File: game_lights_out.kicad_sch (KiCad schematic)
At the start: 91 parts, among them SW1 SW_MEC_5E, SW10 SW_MEC_5E, SW11 SW_MEC_5E, SW12 SW_MEC_5E, SW13 SW_MEC_5E, SW14 SW_MEC_5E, SW15 SW_MEC_5E, SW16 SW_MEC_5E, SW17 SW_MEC_5E, SW18 SW_MEC_5E, SW19 SW_MEC_5E, SW2 SW_MEC_5E, SW20 SW_MEC_5E, SW21 SW_MEC_5E, SW22 SW_MEC_5E, SW23 SW_MEC_5E, SW24 SW_MEC_5E, SW25 SW_MEC_5E, SW26 SW_MEC_5E, SW27 SW_MEC_5E, SW28 SW_MEC_5E, SW29 SW_MEC_5E, SW3 SW_MEC_5E, SW30 SW_MEC_5E, SW31 SW_MEC_5E, SW32 SW_MEC_5E, SW33 SW_MEC_5E, SW34 SW_MEC_5E, SW35 SW_MEC_5E, SW36 SW_MEC_5E, SW37 SW_MEC_5E, SW38 SW_MEC_5E, SW39 SW_MEC_5E, SW4 SW_MEC_5E, SW40 SW_MEC_5E, SW5 SW_MEC_5E, SW6 SW_MEC_5E, SW7 SW_MEC_5E, SW8 SW_MEC_5E, SW9 SW_MEC_5E, U1 ATmega328-P, U2 ULN2803A

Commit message: Added labels to programming pins and updated file format
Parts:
- D1, D10, D11, D12, D13, D14, D15, D16, D17, D18, D19, D2, D20, D21, D22, D23, D24, D25, D26, D27, D28, D29, D3, D30, D31, D32, D33, D34, D35, D36, D37, D38, D39, D4, D40, D5, D6, D7, D8, D9: footprint LED_THT:LED_D5.0mm_IRGrey -> LED_THT:LED_D5.0mm
- DMOD1, DMOD2: footprint LED_THT:LED_D5.0mm_IRGrey -> LED_THT:LED_D1.8mm_W3.3mm_H2.4mm

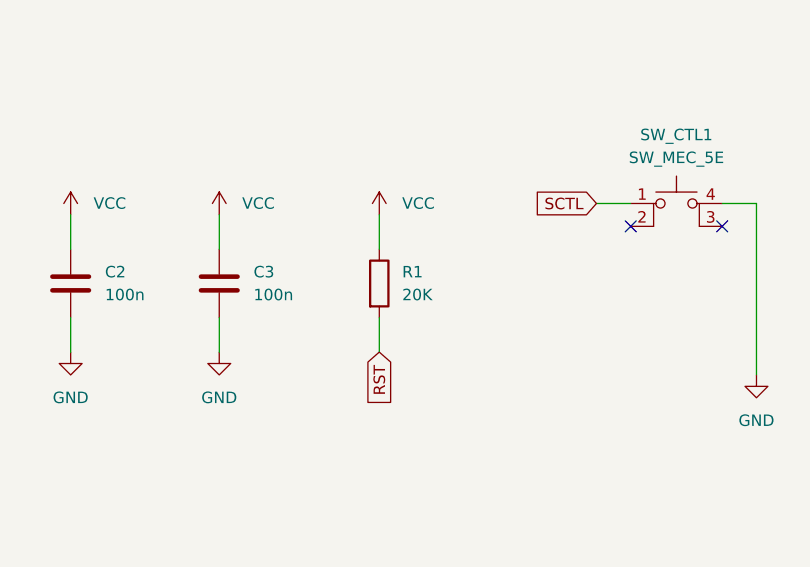
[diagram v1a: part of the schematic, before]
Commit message: Removed reset pin resistor
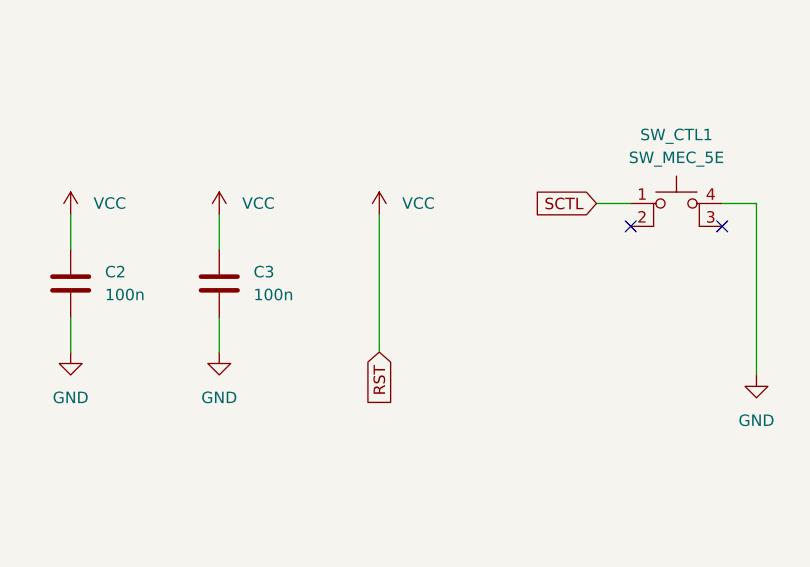
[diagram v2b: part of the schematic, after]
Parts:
- removed R1: 20K, Resistor_THT:R_Axial_DIN0207_L6.3mm_D2.5mm_P7.62mm_Horizontal, symbol Device:R
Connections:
- net RST is gone; now on net VCC: U1.1 (~{RESET}/PC6)
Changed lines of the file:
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@@
     (stroke (width 0) (type default))
   )
+  (wire (pts (xy 194.31 124.46) (xy 194.31 139.7))
+    (stroke (width 0) (type default))
+  )
   (wire (pts (xy 91.44 144.78) (xy 88.9 144.78))
     (stroke (width 0) (type default))
@@
     (stroke (width 0) (type default))
   )
-  (wire (pts (xy 194.31 135.89) (xy 194.31 139.7))
-    (stroke (width 0) (type default))
-  )
   (wire (pts (xy 53.34 129.54) (xy 50.8 129.54))
     (stroke (width 0) (type default))
@@
     (stroke (width 0) (type default))
   )
-  (wire (pts (xy 194.31 124.46) (xy 194.31 128.27))
-    (stroke (width 0) (type default))
-  )
   (wire (pts (xy 114.3 54.61) (xy 115.57 54.61))
     (stroke (width 0) (type default))
@@
         )
       )
-    )
-  )
-  (symbol (lib_id "Device:R") (at 194.31 132.08 0) (unit 1)
-    (in_bom yes) (on_board yes) (dnp no) (fields_autoplaced)
-    (property "Reference" "R1" (at 196.85 130.8099 0)
-      (effects (font (size 1.27 1.27)) (justify left))
-    )
-    (property "Value" "20K" (at 196.85 133.3499 0)
-      (effects (font (size 1.27 1.27)) (justify left))
-    )
-    (property "Footprint" "Resistor_THT:R_Axial_DIN0207_L6.3mm_D2.5mm_P7.62mm_Horizontal" (at 192.532 132.08 90)
-      (effects (font (size 1.27 1.27)) hide)
-    )
-    (property "Datasheet" "~" (at 194.31 132.08 0)
-      (effects (font (size 1.27 1.27)) hide)
-    )
-    (pin "1")
-    (pin "2")
-    (instances
-      (project "game_lights_out"
-        (path "/ccb92925-3037-4924-9354-2881b1b404a5"
-          (reference "R1") (unit 1)
-        )
-      )

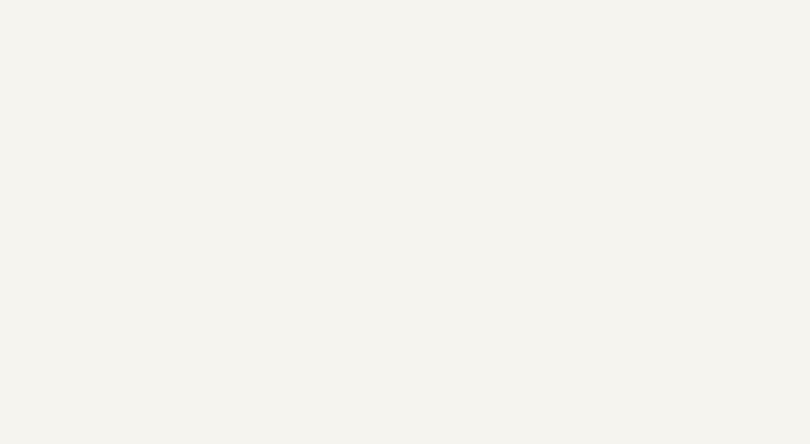
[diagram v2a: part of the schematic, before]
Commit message: Added mounting holes
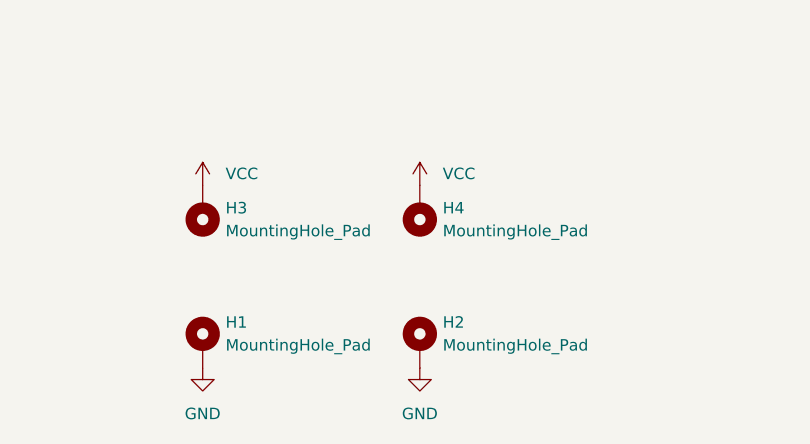
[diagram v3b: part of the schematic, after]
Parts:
- added H1, H2, H3, H4: MountingHole_Pad, MountingHole:MountingHole_2.5mm_Pad, symbol Mechanical:MountingHole_Pad
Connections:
- net GND: now also H1.1, H2.1
- net VCC: now also H3.1, H4.1
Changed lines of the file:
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@@
+    )
+  )
+  (symbol (lib_id "power:VCC") (at 143.51 170.18 0) (unit 1)
+    (in_bom yes) (on_board yes) (dnp no) (fields_autoplaced)
+    (property "Reference" "#PWR02" (at 143.51 173.99 0)
+      (effects (font (size 1.27 1.27)) hide)
+    )
+    (property "Value" "VCC" (at 146.05 168.9099 0)
+      (effects (font (size 1.27 1.27)) (justify left))
+    )
+    (property "Footprint" "" (at 143.51 170.18 0)
+      (effects (font (size 1.27 1.27)) hide)
+    )
+    (property "Datasheet" "" (at 143.51 170.18 0)
+      (effects (font (size 1.27 1.27)) hide)
+    )
+    (pin "1")
+    (instances
+      (project "game_lights_out"
+        (path "/ccb92925-3037-4924-9354-2881b1b404a5"
+          (reference "#PWR02") (unit 1)
+        )
+      )
     )
   )
@@
     )
   )
+  (symbol (lib_id "Mechanical:MountingHole_Pad") (at 143.51 187.96 0) (unit 1)
+    (in_bom yes) (on_board yes) (dnp no) (fields_autoplaced)
+    (property "Reference" "H2" (at 146.05 185.42 0)
+      (effects (font (size 1.27 1.27)) (justify left))
+    )
+    (property "Value" "MountingHole_Pad" (at 146.05 187.96 0)
+      (effects (font (size 1.27 1.27)) (justify left))
+    )
+    (property "Footprint" "MountingHole:MountingHole_2.5mm_Pad" (at 143.51 187.96 0)
+      (effects (font (size 1.27 1.27)) hide)
+    )
+    (property "Datasheet" "~" (at 143.51 187.96 0)
+      (effects (font (size 1.27 1.27)) hide)
+    )
+    (pin "1")
+    (instances
+      (project "game_lights_out"
+        (path "/ccb92925-3037-4924-9354-2881b1b404a5"
+          (reference "H2") (unit 1)
+        )
+      )
+    )
+  )
+  (symbol (lib_id "power:GND") (at 143.51 190.5 0) (unit 1)
+    (in_bom yes) (on_board yes) (dnp no) (fields_autoplaced)
+    (property "Reference" "#PWR04" (at 143.51 196.85 0)
+      (effects (font (size 1.27 1.27)) hide)
+    )
+    (property "Value" "GND" (at 143.51 195.58 0)
+      (effects (font (size 1.27 1.27)))
+    )
+    (property "Footprint" "" (at 143.51 190.5 0)
+      (effects (font (size 1.27 1.27)) hide)
+    )
+    (property "Datasheet" "" (at 143.51 190.5 0)
+      (effects (font (size 1.27 1.27)) hide)
+    )
+    (pin "1")
+    (instances
+      (project "game_lights_out"
+        (path "/ccb92925-3037-4924-9354-2881b1b404a5"
+          (reference "#PWR04") (unit 1)
+        )
+      )
+    )
+  )
   (symbol (lib_id "LED:CQY99") (at 241.3 53.34 270) (unit 1)
     (in_bom yes) (on_board yes) (dnp no) (fields_autoplaced)
@@
     )
   )
+  (symbol (lib_id "power:VCC") (at 119.38 170.18 0) (unit 1)
+    (in_bom yes) (on_board yes) (dnp no) (fields_autoplaced)
+    (property "Reference" "#PWR01" (at 119.38 173.99 0)
+      (effects (font (size 1.27 1.27)) hide)
+    )
+    (property "Value" "VCC" (at 121.92 168.9099 0)
+      (effects (font (size 1.27 1.27)) (justify left))
+    )
+    (property "Footprint" "" (at 119.38 170.18 0)
+      (effects (font (size 1.27 1.27)) hide)
+    )
+    (property "Datasheet" "" (at 119.38 170.18 0)
+      (effects (font (size 1.27 1.27)) hide)
+    )
+    (pin "1")
+    (instances
+      (project "game_lights_out"
+        (path "/ccb92925-3037-4924-9354-2881b1b404a5"
+          (reference "#PWR01") (unit 1)
+        )
+      )
+    )
+  )
   (symbol (lib_id "Switch:SW_MEC_5E") (at 54.61 71.12 0) (unit 1)
     (in_bom yes) (on_board yes) (dnp no) (fields_autoplaced)
@@
         (path "/ccb92925-3037-4924-9354-2881b1b404a5"
           (reference "D27") (unit 1)
+        )
+      )
+    )
+  )
+  (symbol (lib_id "Mechanical:MountingHole_Pad") (at 143.51 172.72 180) (unit 1)
+    (in_bom yes) (on_board yes) (dnp no) (fields_autoplaced)
+    (property "Reference" "H4" (at 146.05 172.72 0)
+      (effects (font (size 1.27 1.27)) (justify right))
+    )
+    (property "Value" "MountingHole_Pad" (at 146.05 175.26 0)
+      (effects (font (size 1.27 1.27)) (justify right))
+    )
+    (property "Footprint" "MountingHole:MountingHole_2.5mm_Pad" (at 143.51 172.72 0)
+      (effects (font (size 1.27 1.27)) hide)
+    )
+    (property "Datasheet" "~" (at 143.51 172.72 0)
+      (effects (font (size 1.27 1.27)) hide)
+    )
+    (pin "1")
+    (instances
+      (project "game_lights_out"
+        (path "/ccb92925-3037-4924-9354-2881b1b404a5"
+          (reference "H4") (unit 1)
         )
       )
@@
     )
   )
+  (symbol (lib_id "Mechanical:MountingHole_Pad") (at 119.38 187.96 0) (unit 1)
+    (in_bom yes) (on_board yes) (dnp no) (fields_autoplaced)
+    (property "Reference" "H1" (at 121.92 185.42 0)
+      (effects (font (size 1.27 1.27)) (justify left))
+    )
+    (property "Value" "MountingHole_Pad" (at 121.92 187.96 0)
+      (effects (font (size 1.27 1.27)) (justify left))
+    )
+    (property "Footprint" "MountingHole:MountingHole_2.5mm_Pad" (at 119.38 187.96 0)
+      (effects (font (size 1.27 1.27)) hide)
+    )
+    (property "Datasheet" "~" (at 119.38 187.96 0)
+      (effects (font (size 1.27 1.27)) hide)
+    )
+    (pin "1")
+    (instances
+      (project "game_lights_out"
+        (path "/ccb92925-3037-4924-9354-2881b1b404a5"
+          (reference "H1") (unit 1)
+        )
+      )
+    )
+  )
   (symbol (lib_id "Switch:SW_MEC_5E") (at 36.83 71.12 0) (unit 1)
     (in_bom yes) (on_board yes) (dnp no) (fields_autoplaced)
@@
     )
   )
+  (symbol (lib_id "power:GND") (at 119.38 190.5 0) (unit 1)
+    (in_bom yes) (on_board yes) (dnp no) (fields_autoplaced)
+    (property "Reference" "#PWR03" (at 119.38 196.85 0)
+      (effects (font (size 1.27 1.27)) hide)
+    )
+    (property "Value" "GND" (at 119.38 195.58 0)
+      (effects (font (size 1.27 1.27)))
+    )
+    (property "Footprint" "" (at 119.38 190.5 0)
+      (effects (font (size 1.27 1.27)) hide)
+    )
+    (property "Datasheet" "" (at 119.38 190.5 0)
+      (effects (font (size 1.27 1.27)) hide)
+    )
+    (pin "1")
+    (instances
+      (project "game_lights_out"
+        (path "/ccb92925-3037-4924-9354-2881b1b404a5"
+          (reference "#PWR03") (unit 1)
+        )
+      )
+    )
+  )
   (symbol (lib_id "Switch:SW_MEC_5E") (at 54.61 29.21 0) (unit 1)
     (in_bom yes) (on_board yes) (dnp no) (fields_autoplaced)
@@
         )
       )
+    )
+  )
+  (symbol (lib_id "Mechanical:MountingHole_Pad") (at 119.38 172.72 180) (unit 1)
+    (in_bom yes) (on_board yes) (dnp no) (fields_autoplaced)
+    (property "Reference" "H3" (at 121.92 172.72 0)
+      (effects (font (size 1.27 1.27)) (justify right))
+    )
+    (property "Value" "MountingHole_Pad" (at 121.92 175.26 0)
+      (effects (font (size 1.27 1.27)) (justify right))
+    )
+    (property "Footprint" "MountingHole:MountingHole_2.5mm_Pad" (at 119.38 172.72 0)
+      (effects (font (size 1.27 1.27)) hide)
+    )
+    (property "Datasheet" "~" (at 119.38 172.72 0)
+      (effects (font (size 1.27 1.27)) hide)
+    )
+    (pin "1")
+    (instances
+      (project "game_lights_out"
+        (path "/ccb92925-3037-4924-9354-2881b1b404a5"
+          (reference "H3") (unit 1)
+        )
+      )

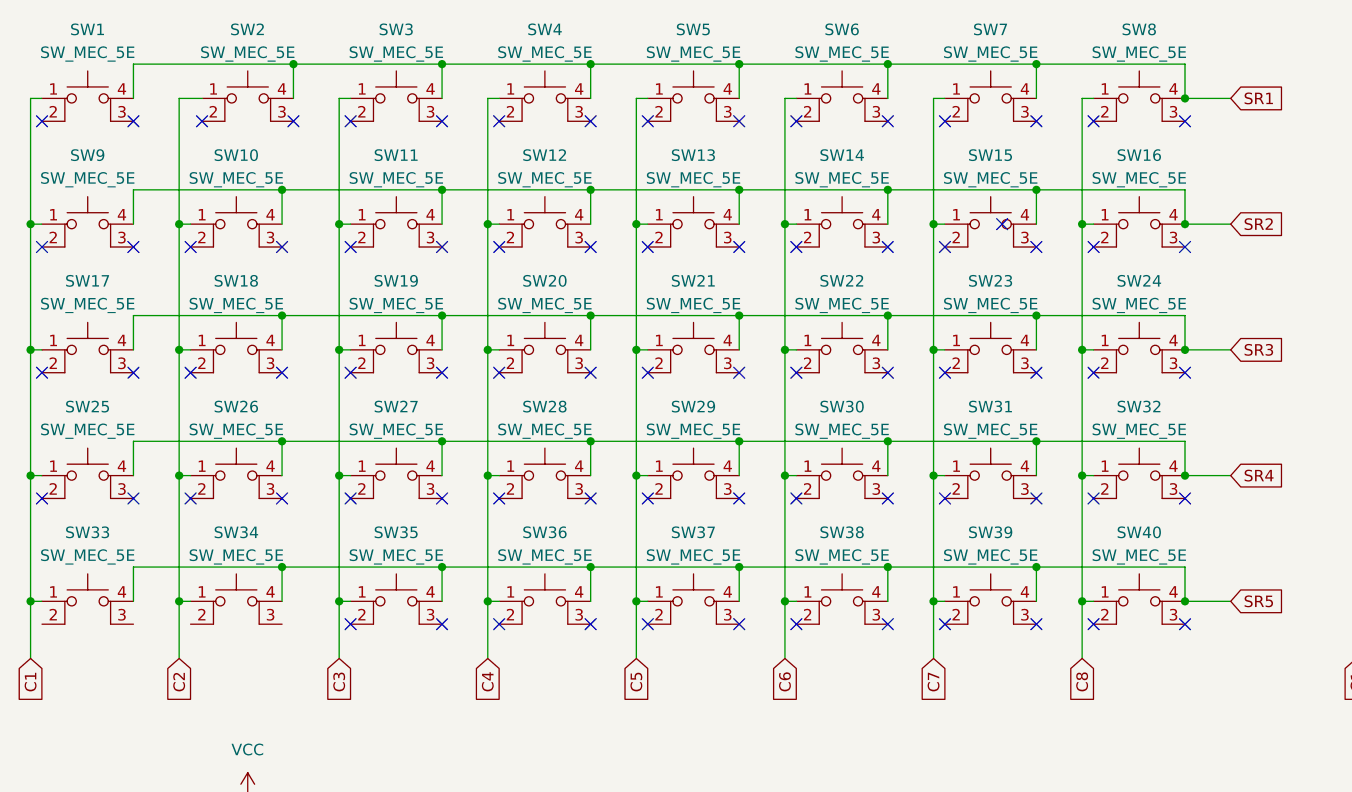
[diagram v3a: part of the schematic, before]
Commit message: Improved switch traces
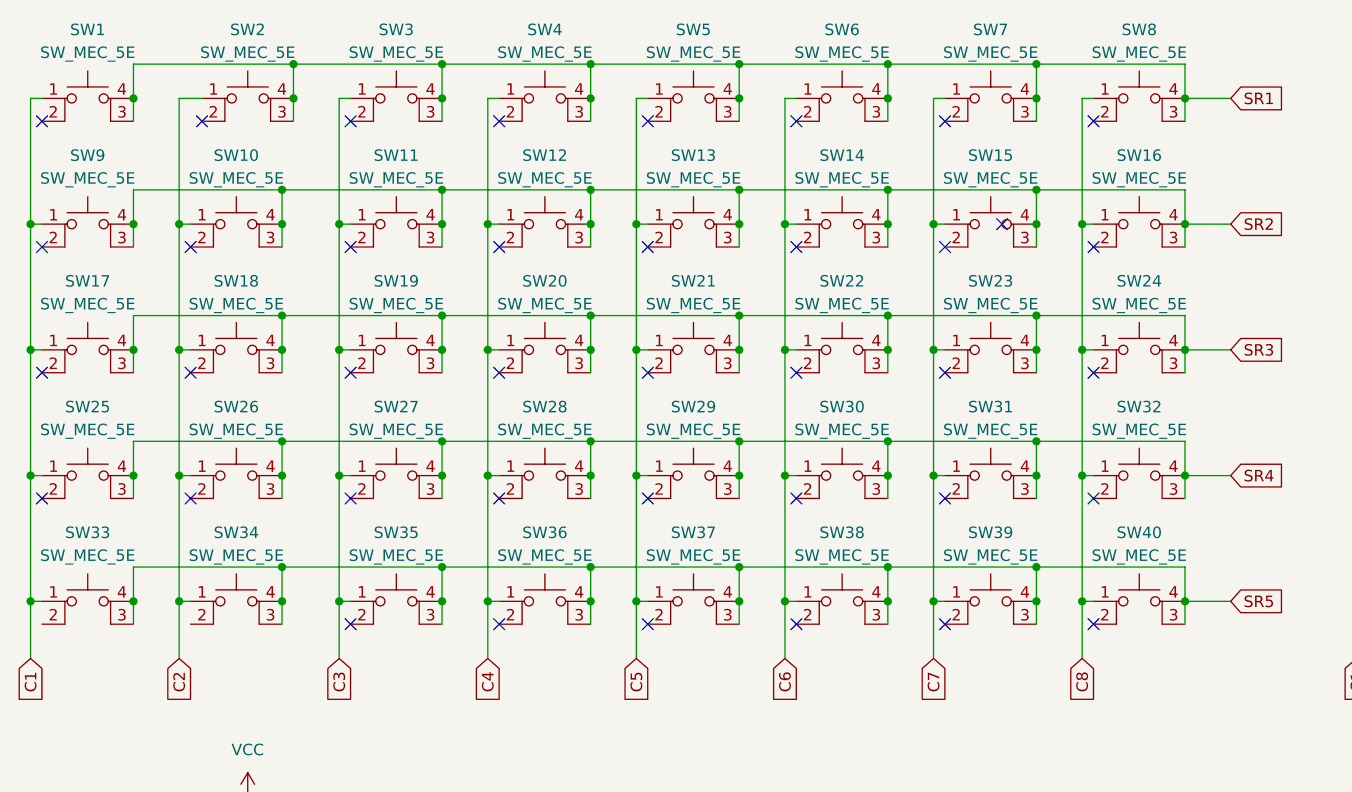
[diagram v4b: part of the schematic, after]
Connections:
- net SR1: now also SW1.3 (K), SW2.3 (K), SW3.3 (K), SW4.3 (K), SW5.3 (K), SW6.3 (K), SW7.3 (K), SW8.3 (K)
- net SR2: now also SW10.3 (K), SW11.3 (K), SW12.3 (K), SW13.3 (K), SW14.3 (K), SW15.3 (K), SW16.3 (K), SW9.3 (K)
- net SR3: now also SW17.3 (K), SW18.3 (K), SW19.3 (K), SW20.3 (K), SW21.3 (K), SW22.3 (K), SW23.3 (K), SW24.3 (K)
- net SR4: now also SW25.3 (K), SW26.3 (K), SW27.3 (K), SW28.3 (K), SW29.3 (K), SW30.3 (K), SW31.3 (K), SW32.3 (K)
- net SR5: now also SW33.3 (K), SW34.3 (K), SW35.3 (K), SW36.3 (K), SW37.3 (K), SW38.3 (K), SW39.3 (K), SW40.3 (K)
- no-connect marks 87 -> 49
